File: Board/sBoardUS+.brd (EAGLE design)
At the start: 50 x 50 mm, 40 parts, among them IC4 MC1525TT

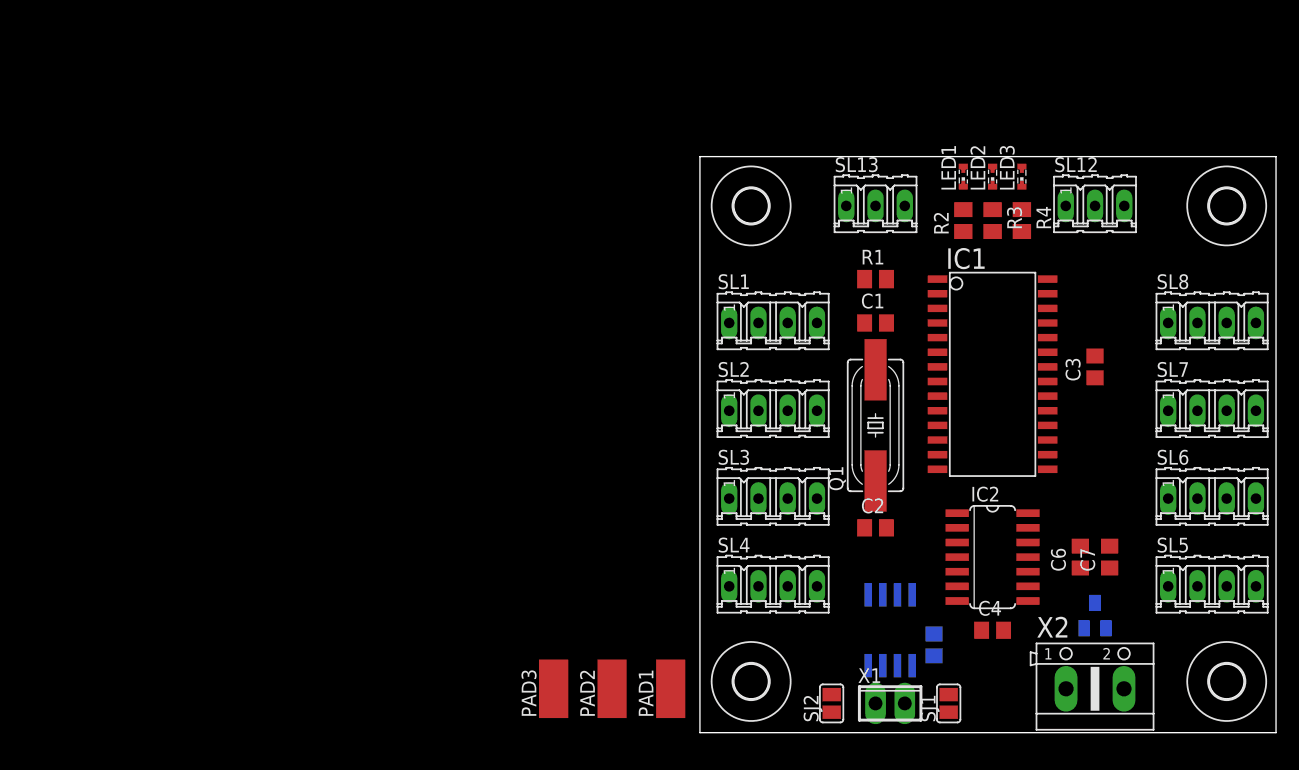
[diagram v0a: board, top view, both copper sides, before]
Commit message: Aggiornamento struttura e modifiche
Cambiata la cartella di lavoro e ricreato il file BRD, modificato lo
schema aggiungendo il led di TX/RX, aggiunto il connettore I2C, cambiato
il quarzo.
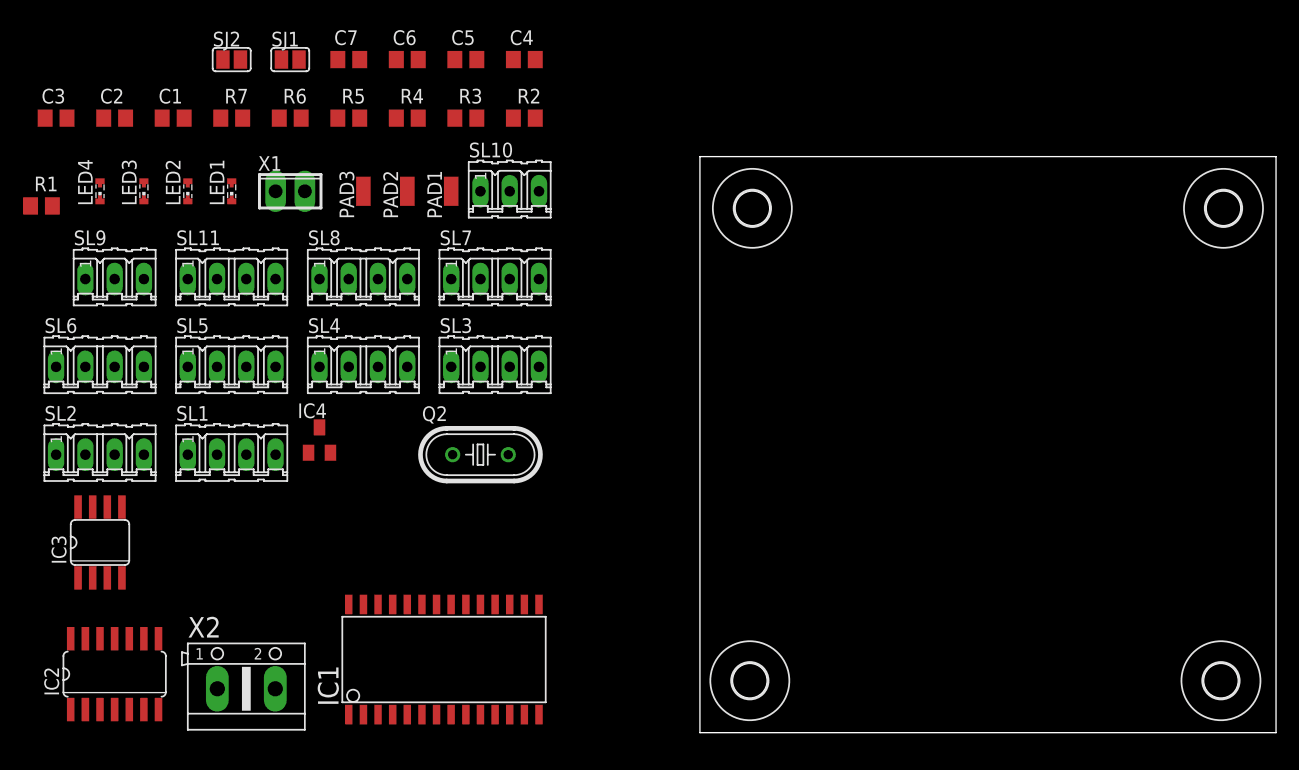
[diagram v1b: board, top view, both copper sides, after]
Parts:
- removed Q1: (no value), crystal:HC49UP
- removed SL12, SL13: (no value), con-amp-quick:03P
- added LED4: (no value), led:SMARTLED-TTW
- added Q2: (no value), crystal:HC49U-V
- added R5, R6, R7: (no value), rcl:R0805
- added SL10, SL9: (no value), con-amp-quick:03P
- added SL11: (no value), con-amp-quick:04P
- PAD1, PAD2, PAD3: device wirepad:SMD2,54-5,08 -> wirepad:SMD1,27-2,54
- R1, R2, R3, R4: device rcl:M2012 -> rcl:R0805
- moved SL6 97.2 mm to (-52.1, 31.8)
- moved C3 92.7 mm to (-55.9, 53.3), turned to 0 degrees
- moved SL5 87.2 mm to (-40.6, 31.8)
- moved SJ1 79.9 mm to (-35.6, 58.4), turned to 0 degrees
- moved C7 78.9 mm to (-30.5, 58.4), turned to 0 degrees
- moved IC2 76.9 mm to (-50.8, 5.08), turned to 0 degrees
- moved SJ2 76.4 mm to (-40.6, 58.4), turned to 0 degrees
- moved LED3 76.2 mm to (-48.3, 47.0)
- moved C2 75.0 mm to (-50.8, 53.3)
- moved SL8 73.8 mm to (-29.2, 39.4)
- moved X2 73.7 mm to (-39.4, 3.81)
- moved R1 72.7 mm to (-57.1, 45.7)
- moved C6 72.6 mm to (-25.4, 58.4), turned to 0 degrees
- moved LED2 69.9 mm to (-44.5, 47.0)
- moved IC4 69.0 mm to (-33.0, 25.4), flipped to the top
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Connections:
- new net N$38: LED4.A@1, R5.2
- new net N$39: IC1.14, R6.2, SL11.3
- new net N$40: IC1.15, R7.2, SL11.2
- net GND: now also LED4.C@1, SL10.1, SL11.1, SL9.1; no longer SL12.1, SL13.1
- net N$1: now also Q2.2; no longer Q1.2
- net N$2: now also Q2.1; no longer Q1.1
- net N$27: now also R5.1
- net N$31: now also R2.1; no longer R2.2
- net N$32: now also R3.1; no longer R3.2
- net N$33: now also R4.1; no longer R4.2
- net N$34: now also R4.2; no longer R4.1
- net N$35: now also R3.2; no longer R3.1
- net N$36: now also R2.2; no longer R2.1
- net N$4: now also R1.2; no longer R1.1
- net N$5: now also SL9.2; no longer SL13.2
- net N$6: now also SL10.2; no longer SL12.2
- net VCC: now also R1.1, R6.1, R7.1, SL10.3, SL11.4, SL9.3; no longer R1.2, SL12.3, SL13.3

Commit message: test
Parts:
- moved SL2 96.7 mm to (44.5, 29.2)
- moved C3 93.3 mm to (34.3, 29.2), turned to 90 degrees
- moved SL1 86.0 mm to (44.5, 36.8)
- moved LED4 82.8 mm to (17.8, 2.54)
- moved C6 81.8 mm to (40.6, 10.2)
- moved R7 81.4 mm to (26.7, 7.62)
- moved IC2 78.3 mm to (26.7, 16.5), turned to 270 degrees
- moved C7 77.8 mm to (30.5, 10.2)
- moved SL4 75.8 mm to (44.5, 14.0)
- moved R1 75.1 mm to (17.8, 40.6), turned to 180 degrees
- moved X2 74.9 mm to (35.6, 3.81)
- moved C2 74.4 mm to (16.5, 21.6)
- moved SL11 73.9 mm to (24.1, 3.81), turned to 180 degrees
- moved LED3 73.7 mm to (25.4, 48.3)
- moved R6 73.2 mm to (21.6, 7.62)
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
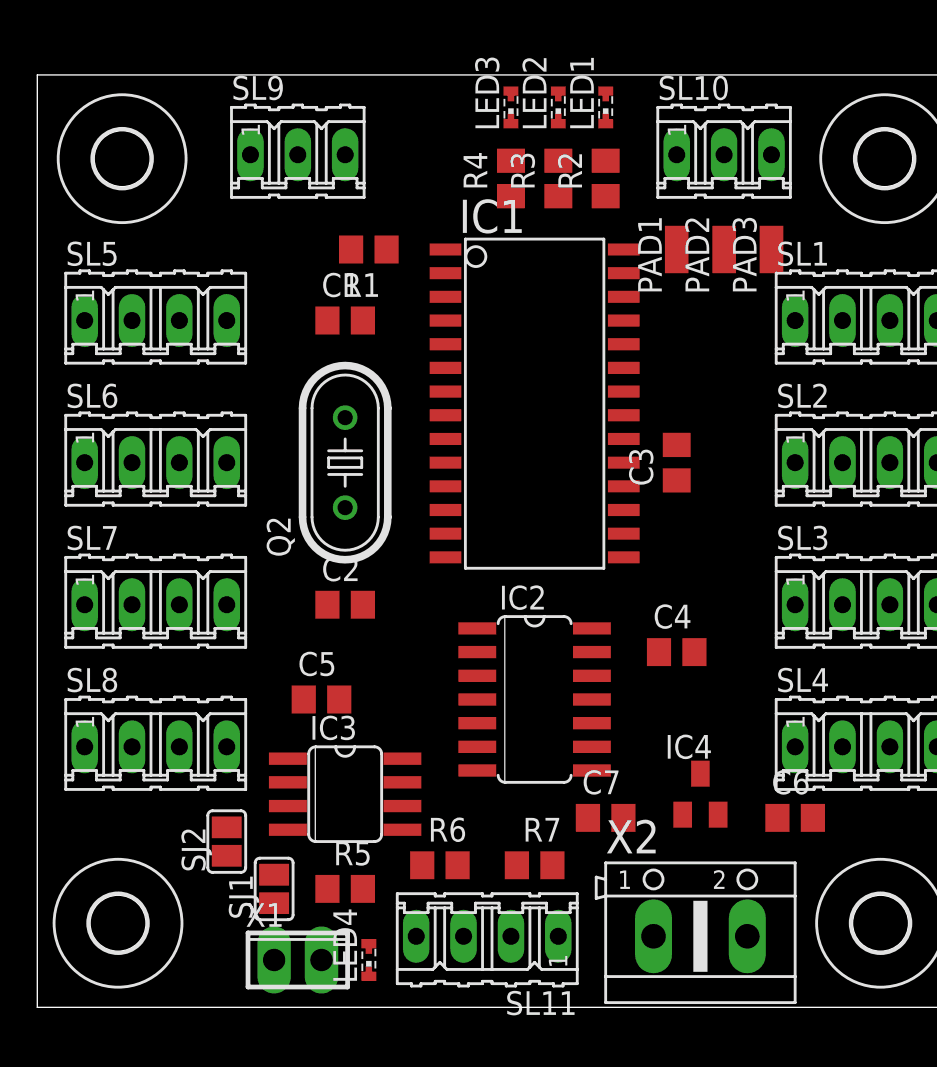
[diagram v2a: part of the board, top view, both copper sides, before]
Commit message: Approntata disposizione
Disposizione non definitiva dei componenti, in particolare per quanto
riguarda i due integrati più piccoli, per il resto dovrebbe essere in un
configurazione ottimale.
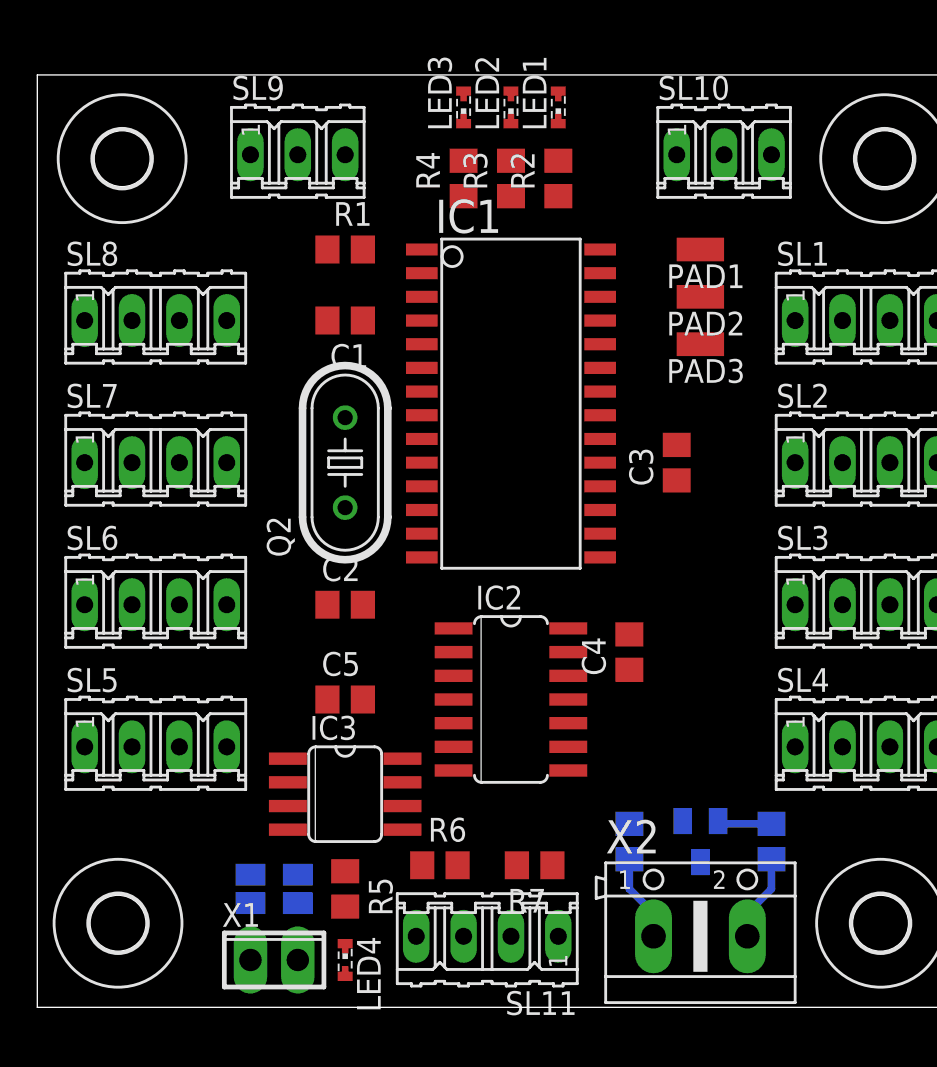
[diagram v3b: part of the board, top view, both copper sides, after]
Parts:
- moved SL5 22.9 mm to (6.35, 14.0)
- moved SL8 22.9 mm to (6.35, 36.8)
- moved C6 8.98 mm to (31.8, 8.89), flipped to the bottom, turned to 90 degrees
- moved C7 8.98 mm to (39.4, 8.89), flipped to the bottom, turned to 270 degrees
- moved SL6 7.62 mm to (6.35, 21.6)
- moved SL7 7.62 mm to (6.35, 29.2)
- moved PAD3 6.35 mm to (35.6, 35.6), turned to 90 degrees
- moved SJ2 2.84 mm to (11.4, 6.35), flipped to the bottom
- moved PAD2 2.84 mm to (35.6, 38.1), turned to 90 degrees
- moved LED2 2.54 mm to (25.4, 48.3)
- moved R3 2.54 mm to (25.4, 44.5)
- moved C4 2.54 mm to (31.8, 19.1), turned to 90 degrees
- moved IC4 2.54 mm to (35.6, 8.89), flipped to the bottom, turned to 180 degrees
- moved LED1 2.54 mm to (27.9, 48.3)
- moved LED3 2.54 mm to (22.9, 48.3)
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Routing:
- net N$37: track 0.00 -> 4.67 mm
- net GND: track 0.00 -> 4.67 mm
- net VCC: track 0.00 -> 2.92 mm

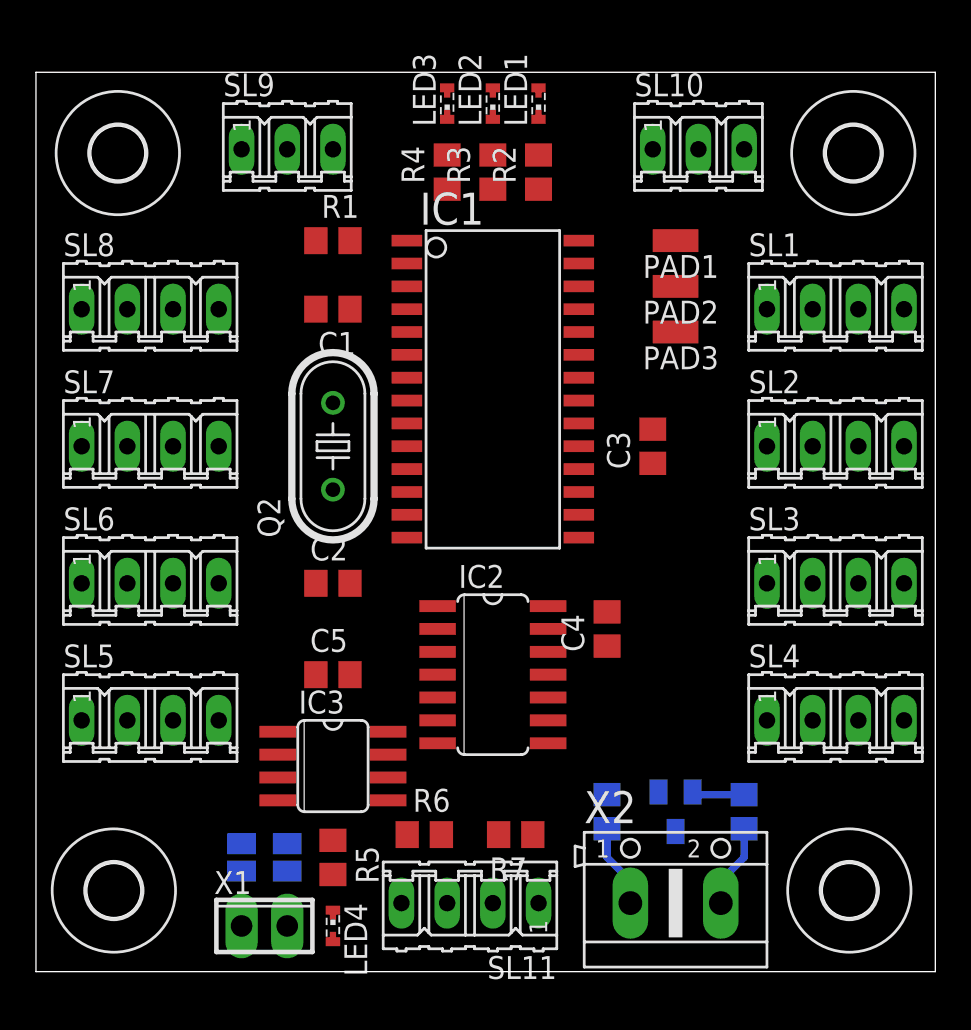
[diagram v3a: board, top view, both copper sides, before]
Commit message: Disegnate alcune piste delle alimentazioni ...
... e riposizionati alcuni componenti per evitare intrecci di piste.
Devo chiedere consiglio per quanto riguarda il posizionamento dei due IC
secondari, trovare il regolatore definitivo e verificare i condenstatori
sul regolatore.
Va anche invertito l'utilizzo delle porte OR in questo modo le piste si
intrecciano troppo.
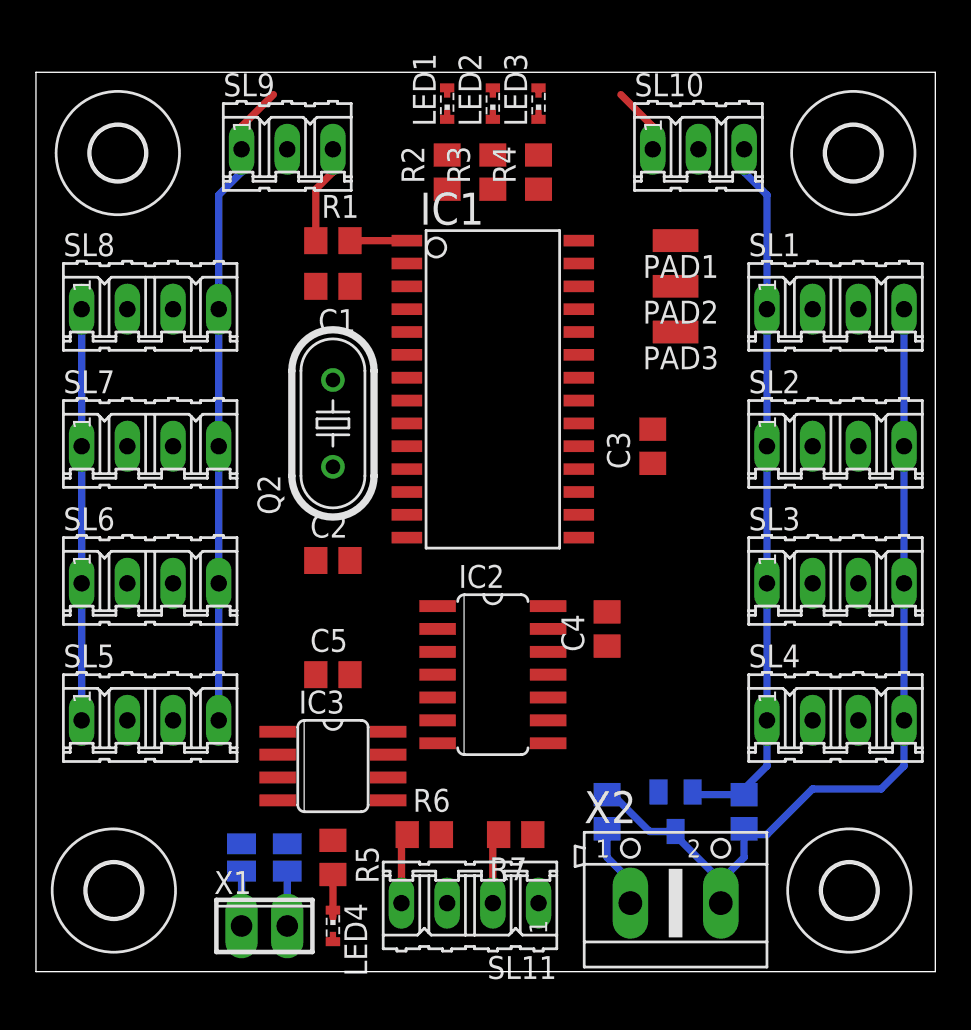
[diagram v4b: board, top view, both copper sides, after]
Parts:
- moved LED1 5.08 mm to (22.9, 48.3)
- moved LED3 5.08 mm to (27.9, 48.3)
- moved R2 5.08 mm to (22.9, 44.5)
- moved R4 5.08 mm to (27.9, 44.5)
- moved C1 1.27 mm to (16.5, 38.1)
- moved C2 1.27 mm to (16.5, 22.9)
- moved Q2 1.27 mm to (16.5, 30.5)
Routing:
- net GND: track 4.67 -> 88.9 mm
- net VCC: track 2.92 -> 72.1 mm
- net N$40: track 0.00 -> 3.94 mm
- net N$4: track 0.00 -> 3.16 mm
- net N$26: track 0.00 -> 3.05 mm
- net N$25: track 0.00 -> 3.05 mm
- net N$38: track 0.00 -> 2.36 mm

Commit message: Invertite le porte OR per ridurre gli incroci delle piste
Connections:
- net N$10: now also IC2.3; no longer IC2.11
- net N$11: now also IC2.5, SL6.3; no longer IC2.2, SL2.3
- net N$12: now also IC2.10, SL4.3; no longer IC2.13, SL8.3
- net N$13: now also IC2.13, SL2.3; no longer IC2.10, SL6.3
- net N$14: now also IC2.1; no longer IC2.12
- net N$15: now also IC2.4; no longer IC2.9
- net N$16: now also IC2.9; no longer IC2.4
- net N$17: now also IC2.12; no longer IC2.1
- net N$3: now also IC2.2, SL8.3; no longer IC2.5, SL4.3
- net N$7: now also IC2.11; no longer IC2.3
- net N$8: now also IC2.8; no longer IC2.6
- net N$9: now also IC2.6; no longer IC2.8
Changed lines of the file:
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@@
 </signal>
 <signal name="N$7">
-<contactref element="IC2" pad="3"/>
 <contactref element="IC1" pad="25"/>
-<wire x1="22.3266" y1="17.78" x2="30.18" y2="36.83" width="0" layer="19" extent="1-1"/>
+<contactref element="IC2" pad="11"/>
+<wire x1="28.4734" y1="16.51" x2="30.18" y2="36.83" width="0" layer="19" extent="1-1"/>
 </signal>
 <signal name="N$8">
 <contactref element="IC1" pad="26"/>
-<contactref element="IC2" pad="6"/>
-<wire x1="22.3266" y1="13.97" x2="30.18" y2="38.1" width="0" layer="19" extent="1-1"/>
+<contactref element="IC2" pad="8"/>
+<wire x1="28.4734" y1="12.7" x2="30.18" y2="38.1" width="0" layer="19" extent="1-1"/>
 </signal>
 <signal name="N$9">
-<contactref element="IC2" pad="8"/>
 <contactref element="IC1" pad="27"/>
 <contactref element="PAD3" pad="1"/>
+<contactref element="IC2" pad="6"/>
 <wire x1="30.18" y1="39.37" x2="35.56" y2="35.56" width="0" layer="19" extent="1-1"/>
-<wire x1="28.4734" y1="12.7" x2="35.56" y2="35.56" width="0" layer="19" extent="1-1"/>
+<wire x1="22.3266" y1="13.97" x2="35.56" y2="35.56" width="0" layer="19" extent="1-1"/>
 </signal>
 <signal name="N$10">
 <contactref element="IC1" pad="28"/>
-<contactref element="IC2" pad="11"/>
 <contactref element="PAD2" pad="1"/>
+<contactref element="IC2" pad="3"/>
 <wire x1="30.18" y1="40.64" x2="35.56" y2="38.1" width="0" layer="19" extent="1-1"/>
-<wire x1="28.4734" y1="16.51" x2="35.56" y2="38.1" width="0" layer="19" extent="1-1"/>
-</signal>
-<signal name="N$12">
-<contactref element="SL8" pad="3"/>
-<contactref element="IC2" pad="13"/>
-<wire x1="7.62" y1="36.83" x2="28.4734" y2="19.05" width="0" layer="19" extent="1-1"/>
-</signal>
-<signal name="N$13">
-<contactref element="IC2" pad="10"/>
-<contactref element="SL6" pad="3"/>
-<wire x1="7.62" y1="21.59" x2="28.4734" y2="15.24" width="0" layer="19" extent="1-1"/>
-</signal>
-<signal name="N$3">
-<contactref element="IC2" pad="5"/>
-<contactref element="SL4" pad="3"/>
-<wire x1="22.3266" y1="15.24" x2="45.72" y2="13.97" width="0" layer="19" extent="1-1"/>
-</signal>
-<signal name="N$11">
-<contactref element="IC2" pad="2"/>
-<contactref element="SL2" pad="3"/>
-<wire x1="22.3266" y1="19.05" x2="45.72" y2="29.21" width="0" layer="19" extent="1-1"/>
+<wire x1="22.3266" y1="17.78" x2="30.18" y2="40.64" width="0" layer="19" extent="1-1"/>
 </signal>
 <signal name="N$14">
 <contactref element="SL7" pad="3"/>
-<contactref element="IC2" pad="12"/>
-<wire x1="7.62" y1="29.21" x2="28.4734" y2="17.78" width="0" layer="19" extent="1-1"/>
+<contactref element="IC2" pad="1"/>
+<wire x1="7.62" y1="29.21" x2="22.3266" y2="20.32" width="0" layer="19" extent="1-1"/>
 </signal>
 <signal name="N$15">
 <contactref element="SL5" pad="3"/>
-<contactref element="IC2" pad="9"/>
-<wire x1="7.62" y1="13.97" x2="28.4734" y2="13.97" width="0" layer="19" extent="1-1"/>
+<contactref element="IC2" pad="4"/>
+<wire x1="7.62" y1="13.97" x2="22.3266" y2="16.51" width="0" layer="19" extent="1-1"/>
 </signal>
 <signal name="N$16">
 <contactref element="SL3" pad="3"/>
-<contactref element="IC2" pad="4"/>
-<wire x1="22.3266" y1="16.51" x2="45.72" y2="21.59" width="0" layer="19" extent="1-1"/>
+<contactref element="IC2" pad="9"/>
+<wire x1="28.4734" y1="13.97" x2="45.72" y2="21.59" width="0" layer="19" extent="1-1"/>
 </signal>
 <signal name="N$17">
 <contactref element="SL1" pad="3"/>
-<contactref element="IC2" pad="1"/>
-<wire x1="22.3266" y1="20.32" x2="45.72" y2="36.83" width="0" layer="19" extent="1-1"/>
+<contactref element="IC2" pad="12"/>
+<wire x1="28.4734" y1="17.78" x2="45.72" y2="36.83" width="0" layer="19" extent="1-1"/>
 </signal>
 <signal name="N$19">
@@
 <wire x1="25.72" y1="7.62" x2="30.18" y2="24.13" width="0" layer="19" extent="1-1"/>
 </signal>
+<signal name="N$3">
+<contactref element="IC2" pad="2"/>
+<contactref element="SL8" pad="3"/>
+<wire x1="22.3266" y1="19.05" x2="7.62" y2="36.83" width="0" layer="19" extent="1-1"/>
+</signal>
+<signal name="N$11">
+<contactref element="SL6" pad="3"/>
+<contactref element="IC2" pad="5"/>
+<wire x1="7.62" y1="21.59" x2="22.3266" y2="15.24" width="0" layer="19" extent="1-1"/>
+</signal>
+<signal name="N$12">
+<contactref element="SL4" pad="3"/>
+<contactref element="IC2" pad="10"/>
+<wire x1="28.4734" y1="15.24" x2="45.72" y2="13.97" width="0" layer="19" extent="1-1"/>
+</signal>
+<signal name="N$13">
+<contactref element="SL2" pad="3"/>
+<contactref element="IC2" pad="13"/>
+<wire x1="28.4734" y1="19.05" x2="45.72" y2="29.21" width="0" layer="19" extent="1-1"/>
+</signal>
 </signals>
